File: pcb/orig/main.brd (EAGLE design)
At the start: 58 x 58 mm, 23 parts, among them Q1 MOSFET-NCHANNEL2N7000

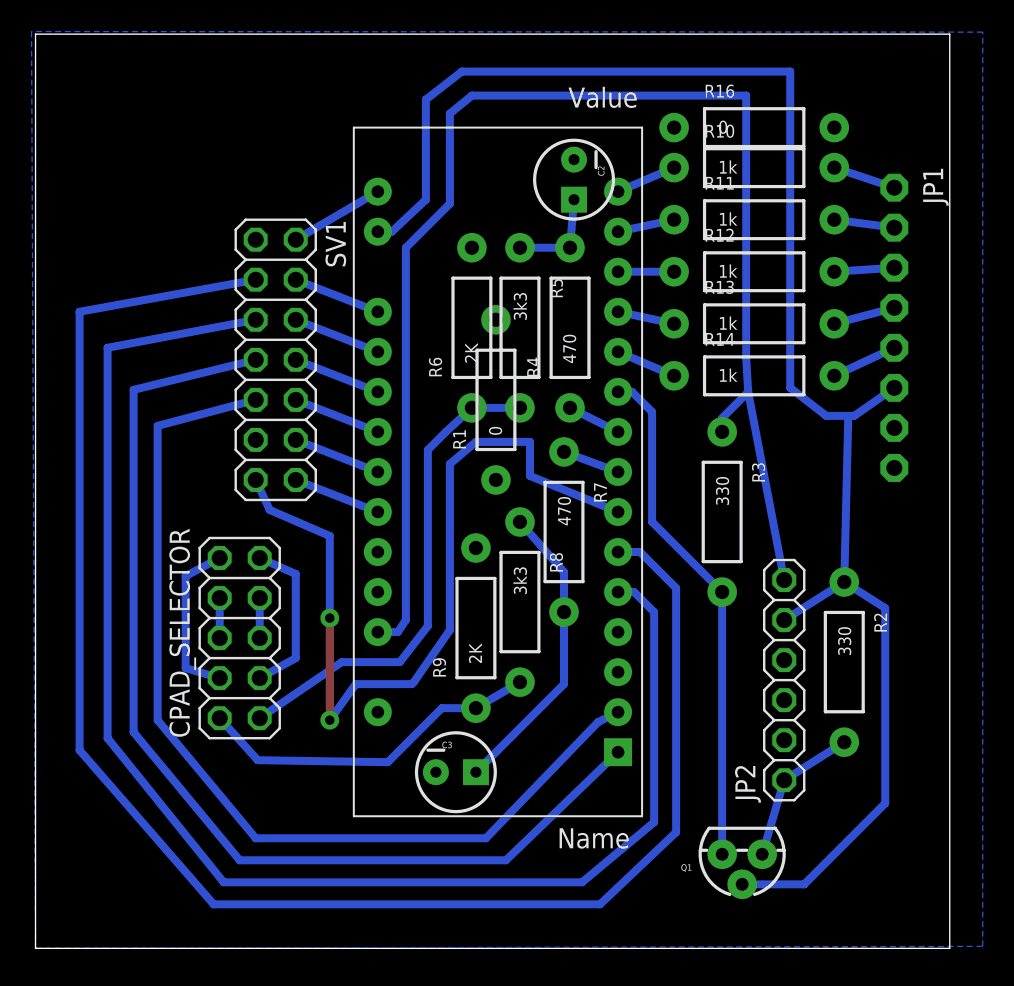
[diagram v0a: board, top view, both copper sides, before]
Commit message: built-in c-pad selector
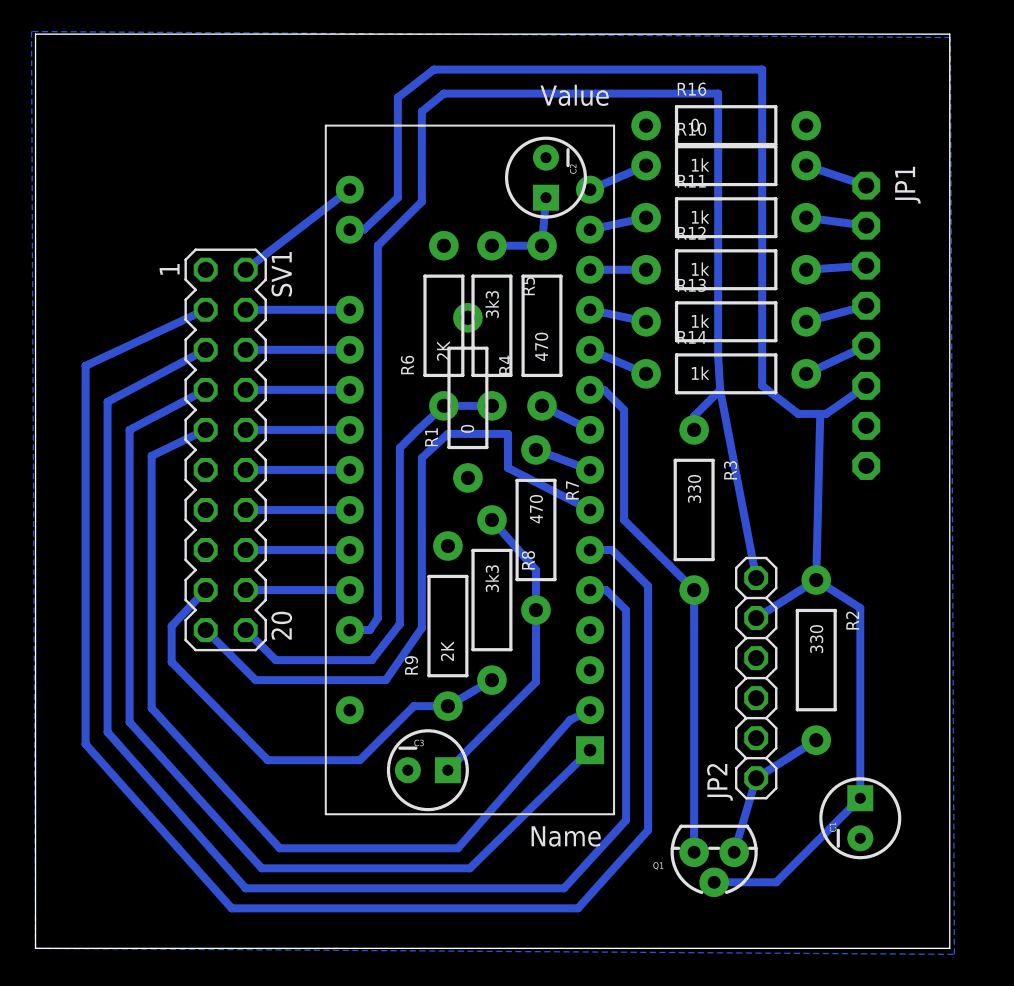
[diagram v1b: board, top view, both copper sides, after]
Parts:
- removed CPAD_SELECTOR: (no value), pinhead:2X05
- added C1: 1uf, SparkFun-Capacitors:CPOL-RADIAL-10UF-25V
- SV1: device pinhead:2X07 -> con-lstb:MA10-2
- moved SV1 6.54 mm to (12.1, 31.6)
- moved Q1 1.78 mm to (43.1, 6.10)
- moved R16 1.78 mm to (43.8, 52.2)
- moved R10 1.78 mm to (43.8, 49.7)
- moved R11 1.78 mm to (43.8, 46.4)
- moved R12 1.78 mm to (43.8, 43.1)
- moved R13 1.78 mm to (43.8, 39.8)
- moved R14 1.78 mm to (43.8, 36.4)
- moved C3 1.78 mm to (24.9, 11.3)
- moved R5 1.78 mm to (29.0, 39.5)
- moved R8 1.78 mm to (29.0, 22.1)
- moved R9 1.78 mm to (26.2, 20.4)
- moved R1 1.78 mm to (27.4, 34.9)
- moved C2 1.78 mm to (32.4, 48.9)
- moved JP1 1.78 mm to (52.7, 39.5)
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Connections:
- removed net DS_ANALOG_IN_X: CPAD_SELECTOR.3, CPAD_SELECTOR.9
- removed net DS_ANALOG_IN_Y: CPAD_SELECTOR.10, CPAD_SELECTOR.4
- removed net DS_CPAD_OUTX: CPAD_SELECTOR.5, CPAD_SELECTOR.7
- removed net DS_CPAD_OUT_Y: CPAD_SELECTOR.6, CPAD_SELECTOR.8
- new net N$15: SV1.16, U$1.A6
- new net N$16: SV1.18, U$1.A7
- net 3.3V: now also C1.1
- net CPAD_X_1V8: now also SV1.20; no longer CPAD_SELECTOR.1
- net CPAD_Y_1V8: now also SV1.17; no longer CPAD_SELECTOR.2
- net GND: now also C1.2
- net N$18: now also SV1.19; no longer SV1.13
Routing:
- net N$18: track 52.8 -> 41.6 mm, vias 2 -> 0
- net DS_ANALOG_IN_Y: track 10.5 -> 0.00 mm
- net DS_ANALOG_IN_X: track 10.5 -> 0.00 mm
- net N$19: track 103.4 -> 95.1 mm
- net CPAD_Y_1V8: track 22.1 -> 30.2 mm
- net N$20: track 90.9 -> 83.4 mm
- net N$21: track 67.0 -> 60.4 mm
- net N$16: track 0.00 -> 6.60 mm
- net N$15: track 0.00 -> 6.60 mm
- net N$22: track 61.1 -> 55.4 mm
- net DS_CPAD_OUT_Y: track 2.54 -> 0.00 mm
- net DS_CPAD_OUTX: track 2.54 -> 0.00 mm
- net N$8: track 6.03 -> 8.33 mm
- net CPAD_X_1V8: track 31.0 -> 29.8 mm
- net N$14: track 5.59 -> 6.60 mm
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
